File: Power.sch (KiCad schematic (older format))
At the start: 15 parts, among them P4 CONN_01X03, U10 RT9183, U9 TPS799

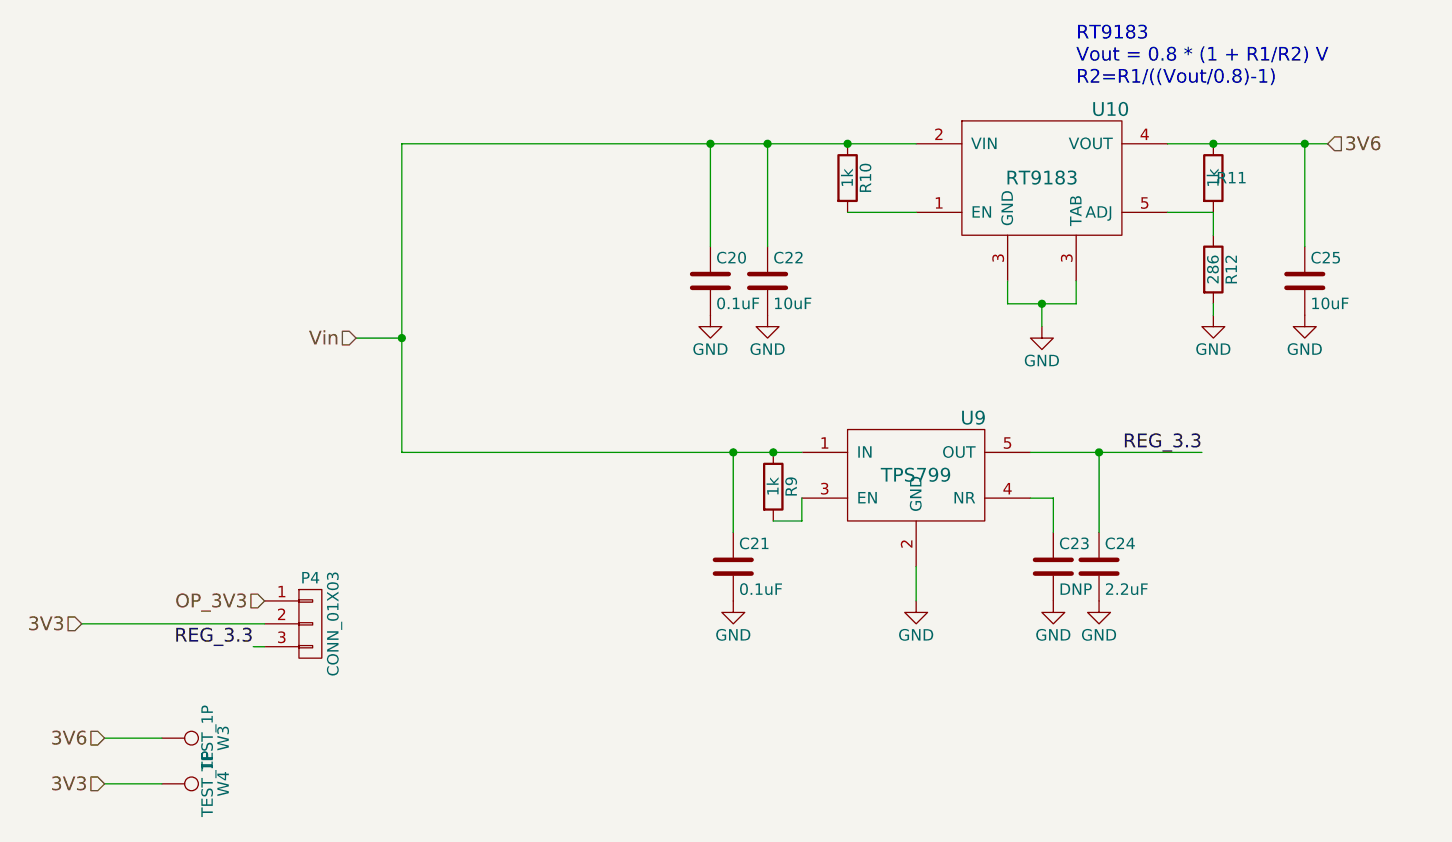
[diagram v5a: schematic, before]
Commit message: Updated schematic and layout
Added extra decoupling caps based on TI feedback and forward annotated changes to the PCB
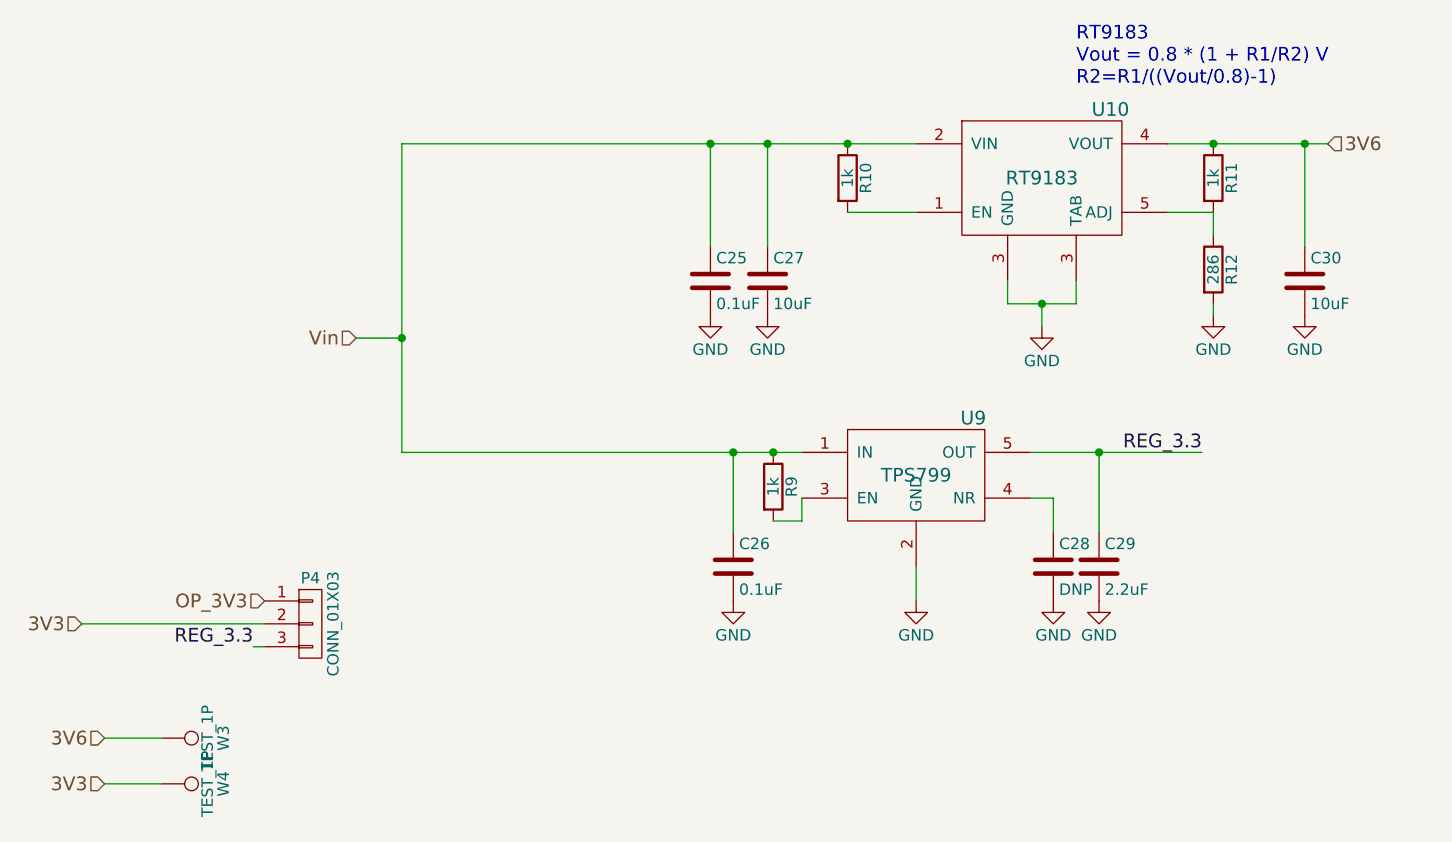
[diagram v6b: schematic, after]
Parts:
- W3, W4: footprint SFUSat:EXPOSED -> SFUSat:Measurement_Point_Round-SMD-Pad_Big
- renumbered C20 to C25, C21 to C26, C22 to C27, C23 to C28, C24 to C29, C25 to C30
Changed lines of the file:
@@
 EESchema Schematic File Version 2
+LIBS:SFUSat-Radio-rescue
 LIBS:power
 LIBS:device
@@
 $EndComp
 $Comp
-L C C22
+L C C27
 U 1 1 587706B0
 P 5700 2600
-F 0 "C22" H 5725 2700 50  0000 L CNN
+F 0 "C27" H 5725 2700 50  0000 L CNN
 F 1 "10uF" H 5725 2500 50  0000 L CNN
 F 2 "SFUSat:C_0402" H 5738 2450 50  0001 C CNN
@@
 $EndComp
 $Comp
-L C C20
+L C C25
 U 1 1 58770789
 P 5450 2600
-F 0 "C20" H 5475 2700 50  0000 L CNN
+F 0 "C25" H 5475 2700 50  0000 L CNN
 F 1 "0.1uF" H 5475 2500 50  0000 L CNN
 F 2 "SFUSat:C_0402" H 5488 2450 50  0001 C CNN
@@
 $EndComp
 $Comp
-L GND #PWR036
+L GND #PWR041
 U 1 1 58770941
 P 6900 2800
-F 0 "#PWR036" H 6900 2550 50  0001 C CNN
+F 0 "#PWR041" H 6900 2550 50  0001 C CNN
 F 1 "GND" H 6900 2650 50  0000 C CNN
 F 2 "" H 6900 2800 50  0000 C CNN
@@
 $EndComp
 $Comp
-L C C25
+L C C30
 U 1 1 58770AC4
 P 8050 2600
-F 0 "C25" H 8075 2700 50  0000 L CNN
+F 0 "C30" H 8075 2700 50  0000 L CNN
 F 1 "10uF" H 8075 2500 50  0000 L CNN
 F 2 "SFUSat:C_0402" H 8088 2450 50  0001 C CNN
@@
 $EndComp
 $Comp
-L GND #PWR037
+L GND #PWR042
 U 1 1 58770B93
 P 8050 2750
-F 0 "#PWR037" H 8050 2500 50  0001 C CNN
+F 0 "#PWR042" H 8050 2500 50  0001 C CNN
 F 1 "GND" H 8050 2600 50  0000 C CNN
 F 2 "" H 8050 2750 50  0000 C CNN
@@
 $EndComp
 $Comp
-L GND #PWR038
+L GND #PWR043
 U 1 1 58770BD7
 P 7650 2750
-F 0 "#PWR038" H 7650 2500 50  0001 C CNN
+F 0 "#PWR043" H 7650 2500 50  0001 C CNN
 F 1 "GND" H 7650 2600 50  0000 C CNN
 F 2 "" H 7650 2750 50  0000 C CNN
@@
 $EndComp
 $Comp
-L GND #PWR039
+L GND #PWR044
 U 1 1 58770CCB
 P 5700 2750
-F 0 "#PWR039" H 5700 2500 50  0001 C CNN
+F 0 "#PWR044" H 5700 2500 50  0001 C CNN
 F 1 "GND" H 5700 2600 50  0000 C CNN
 F 2 "" H 5700 2750 50  0000 C CNN
@@
 $EndComp
 $Comp
-L GND #PWR040
+L GND #PWR045
 U 1 1 58770CE7
 P 5450 2750
-F 0 "#PWR040" H 5450 2500 50  0001 C CNN
+F 0 "#PWR045" H 5450 2500 50  0001 C CNN
 F 1 "GND" H 5450 2600 50  0000 C CNN
 F 2 "" H 5450 2750 50  0000 C CNN
@@
 U 1 1 58770EC5
 P 7650 2150
-F 0 "R11" H 7730 2150 50  0000 C CNN
+F 0 "R11" V 7730 2150 50  0000 C CNN
 F 1 "1k" V 7650 2150 50  0000 C CNN
 F 2 "SFUSat:R_0402" V 7580 2150 50  0001 C CNN
@@
 $EndComp
 $Comp
-L GND #PWR041
+L GND #PWR046
 U 1 1 5879D9E2
 P 6350 4000
-F 0 "#PWR041" H 6350 3750 50  0001 C CNN
+F 0 "#PWR046" H 6350 3750 50  0001 C CNN
 F 1 "GND" H 6350 3850 50  0000 C CNN
 F 2 "" H 6350 4000 50  0000 C CNN
@@
 $EndComp
 $Comp
-L GND #PWR042
+L GND #PWR047
 U 1 1 5879DA04
 P 7150 4000
-F 0 "#PWR042" H 7150 3750 50  0001 C CNN
+F 0 "#PWR047" H 7150 3750 50  0001 C CNN
 F 1 "GND" H 7150 3850 50  0000 C CNN
 F 2 "" H 7150 4000 50  0000 C CNN
@@
 $EndComp
 $Comp
-L GND #PWR043
+L GND #PWR048
 U 1 1 5879DA26
 P 6950 4000
-F 0 "#PWR043" H 6950 3750 50  0001 C CNN
+F 0 "#PWR048" H 6950 3750 50  0001 C CNN
 F 1 "GND" H 6950 3850 50  0000 C CNN
 F 2 "" H 6950 4000 50  0000 C CNN
@@
 $EndComp
 $Comp
-L C C23
+L C C28
 U 1 1 5879DA48
 P 6950 3850
-F 0 "C23" H 6975 3950 50  0000 L CNN
+F 0 "C28" H 6975 3950 50  0000 L CNN
 F 1 "DNP" H 6975 3750 50  0000 L CNN
 F 2 "SFUSat:C_0402" H 6988 3700 50  0001 C CNN
@@
 $EndComp
 $Comp
-L C C24
+L C C29
 U 1 1 5879DAAB
 P 7150 3850
-F 0 "C24" H 7175 3950 50  0000 L CNN
+F 0 "C29" H 7175 3950 50  0000 L CNN
 F 1 "2.2uF" H 7175 3750 50  0000 L CNN
 F 2 "SFUSat:C_0402" H 7188 3700 50  0001 C CNN
@@
 $EndComp
 $Comp
-L GND #PWR044
+L GND #PWR049
 U 1 1 5879E264
 P 5550 4000
-F 0 "#PWR044" H 5550 3750 50  0001 C CNN
+F 0 "#PWR049" H 5550 3750 50  0001 C CNN
 F 1 "GND" H 5550 3850 50  0000 C CNN
 F 2 "" H 5550 4000 50  0000 C CNN
@@
 $EndComp
 $Comp
-L C C21
+L C C26
 U 1 1 5879E323
 P 5550 3850
-F 0 "C21" H 5575 3950 50  0000 L CNN
+F 0 "C26" H 5575 3950 50  0000 L CNN
 F 1 "0.1uF" H 5575 3750 50  0000 L CNN
 F 2 "SFUSat:C_0402" H 5588 3700 50  0001 C CNN
@@
 F 0 "W3" H 3050 4870 50  0000 C CNN
 F 1 "TEST_1P" H 3050 4800 50  0000 C CNN
-F 2 "SFUSat:EXPOSED" H 3250 4600 50  0001 C CNN
+F 2 "SFUSat:Measurement_Point_Round-SMD-Pad_Big" H 3250 4600 50  0001 C CNN
 F 3 "" H 3250 4600 50  0000 C CNN
 	1    3050 4600
@@
 F 0 "W4" H 3050 5070 50  0000 C CNN
 F 1 "TEST_1P" H 3050 5000 50  0000 C CNN
-F 2 "SFUSat:EXPOSED" H 3250 4800 50  0001 C CNN
+F 2 "SFUSat:Measurement_Point_Round-SMD-Pad_Big" H 3250 4800 50  0001 C CNN
 F 3 "" H 3250 4800 50  0000 C CNN
 	1    3050 4800

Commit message: Changed C25 and C26 from 0.1uF to 100nF
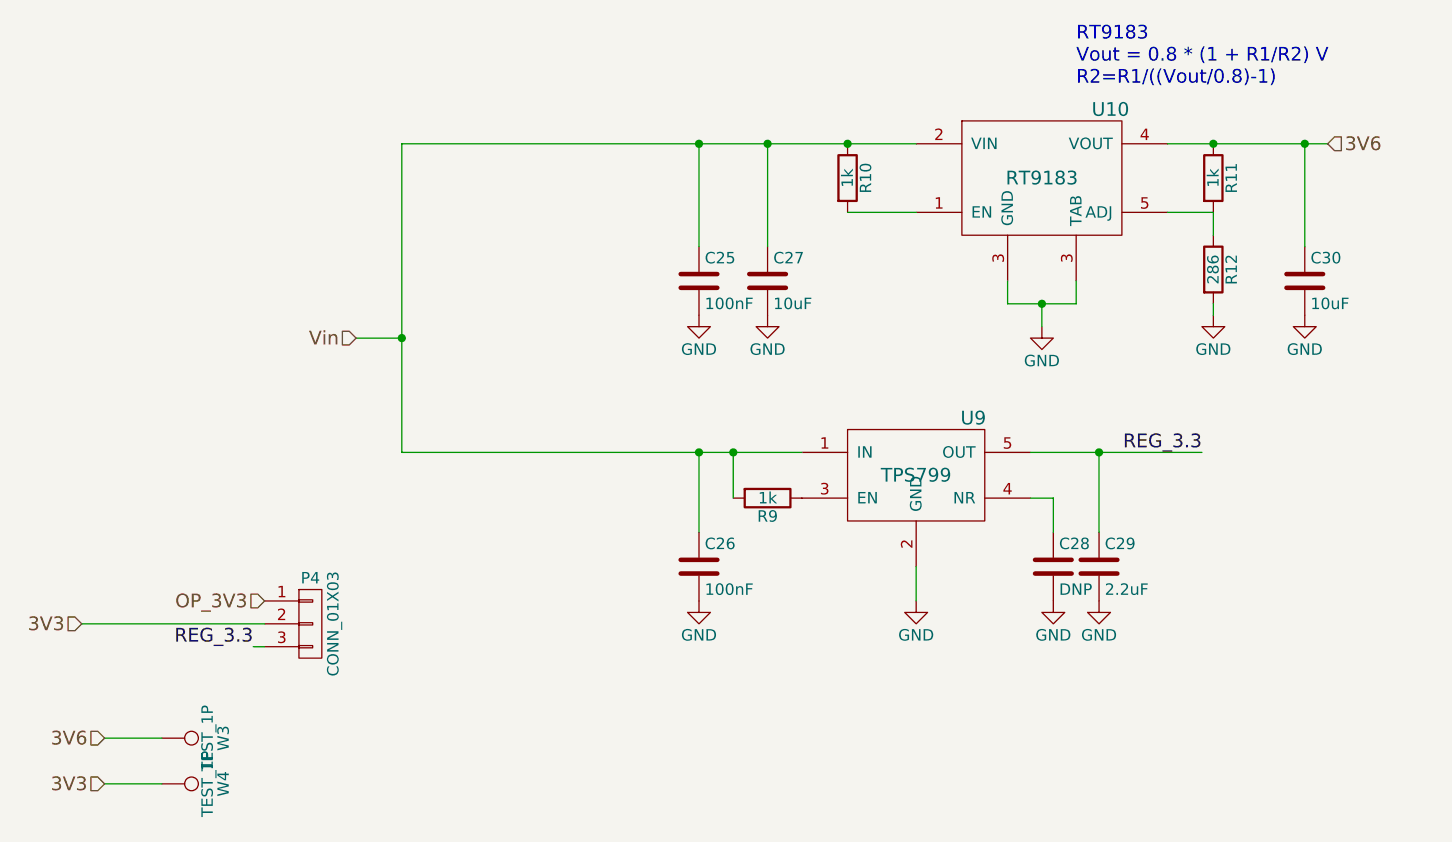
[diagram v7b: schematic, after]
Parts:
- C25, C26: value 0.1uF -> 100nF
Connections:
- net Vin: now also R9.2; no longer R9.1
- net at U9.3 (EN): now also R9.1; no longer R9.2
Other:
- moved on the sheet: C25, C26, R9
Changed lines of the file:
@@
 EESchema Schematic File Version 2
-LIBS:SFUSat-Radio-rescue
 LIBS:power
 LIBS:device
@@
 L C C25
 U 1 1 58770789
-P 5450 2600
-F 0 "C25" H 5475 2700 50  0000 L CNN
-F 1 "0.1uF" H 5475 2500 50  0000 L CNN
-F 2 "SFUSat:C_0402" H 5488 2450 50  0001 C CNN
-F 3 "" H 5450 2600 50  0000 C CNN
-	1    5450 2600
+P 5400 2600
+F 0 "C25" H 5425 2700 50  0000 L CNN
+F 1 "100nF" H 5425 2500 50  0000 L CNN
+F 2 "SFUSat:C_0402" H 5438 2450 50  0001 C CNN
+F 3 "" H 5400 2600 50  0000 C CNN
+	1    5400 2600
 	1    0    0    -1
 $EndComp
@@
 L GND #PWR045
 U 1 1 58770CE7
-P 5450 2750
-F 0 "#PWR045" H 5450 2500 50  0001 C CNN
-F 1 "GND" H 5450 2600 50  0000 C CNN
-F 2 "" H 5450 2750 50  0000 C CNN
-F 3 "" H 5450 2750 50  0000 C CNN
-	1    5450 2750
+P 5400 2750
+F 0 "#PWR045" H 5400 2500 50  0001 C CNN
+F 1 "GND" H 5400 2600 50  0000 C CNN
+F 2 "" H 5400 2750 50  0000 C CNN
+F 3 "" H 5400 2750 50  0000 C CNN
+	1    5400 2750
 	1    0    0    -1
 $EndComp
@@
 L GND #PWR049
 U 1 1 5879E264
-P 5550 4000
-F 0 "#PWR049" H 5550 3750 50  0001 C CNN
-F 1 "GND" H 5550 3850 50  0000 C CNN
-F 2 "" H 5550 4000 50  0000 C CNN
-F 3 "" H 5550 4000 50  0000 C CNN
-	1    5550 4000
+P 5400 4000
+F 0 "#PWR049" H 5400 3750 50  0001 C CNN
+F 1 "GND" H 5400 3850 50  0000 C CNN
+F 2 "" H 5400 4000 50  0000 C CNN
+F 3 "" H 5400 4000 50  0000 C CNN
+	1    5400 4000
 	1    0    0    -1
 $EndComp
@@
 L C C26
 U 1 1 5879E323
-P 5550 3850
-F 0 "C26" H 5575 3950 50  0000 L CNN
-F 1 "0.1uF" H 5575 3750 50  0000 L CNN
-F 2 "SFUSat:C_0402" H 5588 3700 50  0001 C CNN
-F 3 "" H 5550 3850 50  0000 C CNN
-	1    5550 3850
+P 5400 3850
+F 0 "C26" H 5425 3950 50  0000 L CNN
+F 1 "100nF" H 5425 3750 50  0000 L CNN
+F 2 "SFUSat:C_0402" H 5438 3700 50  0001 C CNN
+F 3 "" H 5400 3850 50  0000 C CNN
+	1    5400 3850
 	1    0    0    -1
 $EndComp
@@
 	1    0    0    -1
 $EndComp
+Wire Wire Line
+	4100 2000 6350 2000
+Connection ~ 5700 2000
+Wire Wire Line
+	6750 2600 6750 2700
+Wire Wire Line
+	7050 2600 7050 2700
+Wire Wire Line
+	7050 2700 6750 2700
+Wire Wire Line
+	6900 2700 6900 2800
+Connection ~ 6900 2700
+Wire Wire Line
+	8050 2000 8050 2450
+Connection ~ 8050 2000
+Wire Wire Line
+	7450 2300 7650 2300
+Wire Wire Line
+	7650 2300 7650 2400
+Wire Wire Line
+	7650 2750 7650 2700
+Wire Wire Line
+	6350 3850 6350 4000
+Wire Wire Line
+	6850 3550 6950 3550
+Wire Wire Line
+	6950 3550 6950 3700
+Wire Wire Line
+	6850 3350 7600 3350
+Wire Wire Line
+	7150 3350 7150 3700
+Connection ~ 7150 3350
+Wire Wire Line
+	5400 3350 5400 3700
+Wire Wire Line
+	4100 2850 3900 2850
+Connection ~ 4100 2850
+Wire Wire Line
+	5700 2450 5700 2000
+Wire Wire Line
+	6350 2300 6050 2300
+Connection ~ 6050 2000
+Wire Wire Line
+	4100 2000 4100 3350
+Wire Wire Line
+	3500 4200 3450 4200
+Wire Wire Line
+	3500 4100 2700 4100
+Wire Wire Line
+	2800 4600 3050 4600
+Wire Wire Line
+	2800 4800 3050 4800
+Wire Wire Line
+	7450 2000 8150 2000
+Connection ~ 7650 2000
+Wire Wire Line
+	5400 2450 5400 2000
+Connection ~ 5400 2000
 $Comp
 L R R9
 U 1 1 58948796
-P 5725 3500
-F 0 "R9" V 5805 3500 50  0000 C CNN
-F 1 "1k" V 5725 3500 50  0000 C CNN
-F 2 "SFUSat:R_0402" V 5655 3500 50  0001 C CNN
-F 3 "" H 5725 3500 50  0000 C CNN
-	1    5725 3500
-	1    0    0    -1
-$EndComp
-Wire Wire Line
-	4100 2000 6350 2000
-Connection ~ 5700 2000
-Wire Wire Line
-	6750 2600 6750 2700
-Wire Wire Line
-	7050 2600 7050 2700
-Wire Wire Line
-	7050 2700 6750 2700
-Wire Wire Line
-	6900 2700 6900 2800
-Connection ~ 6900 2700
-Wire Wire Line
-	8050 2000 8050 2450
-Connection ~ 8050 2000
-Wire Wire Line
-	7450 2300 7650 2300
-Wire Wire Line
-	7650 2300 7650 2400
-Wire Wire Line
-	7650 2750 7650 2700
-Wire Wire Line
-	6350 3850 6350 4000
-Wire Wire Line
-	6850 3550 6950 3550
-Wire Wire Line
-	6950 3550 6950 3700
-Wire Wire Line
-	6850 3350 7600 3350
-Wire Wire Line
-	7150 3350 7150 3700
-Connection ~ 7150 3350
-Wire Wire Line
-	5550 3350 5550 3700
+P 5700 3550
+F 0 "R9" V 5780 3550 50  0000 C CNN
+F 1 "1k" V 5700 3550 50  0000 C CNN
+F 2 "SFUSat:R_0402" V 5630 3550 50  0001 C CNN
+F 3 "" H 5700 3550 50  0000 C CNN
+	1    5700 3550
+	0    1    1    0
+$EndComp
+Wire Wire Line
+	5550 3550 5550 3350
+Wire Wire Line
+	4100 3350 5850 3350
 Connection ~ 5550 3350
-Wire Wire Line
-	4100 2850 3900 2850
-Connection ~ 4100 2850
-Wire Wire Line
-	5700 2450 5700 2000
-Wire Wire Line
-	5450 2450 5450 2000
-Connection ~ 5450 2000
-Wire Wire Line
-	6350 2300 6050 2300
-Connection ~ 6050 2000
-Wire Wire Line
-	4100 2000 4100 3350
-Wire Wire Line
-	3500 4200 3450 4200
-Wire Wire Line
-	3500 4100 2700 4100
-Wire Wire Line
-	2800 4600 3050 4600
-Wire Wire Line
-	2800 4800 3050 4800
-Wire Wire Line
-	7450 2000 8150 2000
-Connection ~ 7650 2000
-Wire Wire Line
-	5850 3550 5850 3650
-Wire Wire Line
-	5850 3650 5725 3650
-Wire Wire Line
-	4100 3350 5850 3350
-Connection ~ 5725 3350
+Connection ~ 5400 3350
 $EndSCHEMATC
